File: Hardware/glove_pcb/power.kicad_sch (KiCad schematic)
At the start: 16 parts, among them J1 Barrel_Jack_Switch, U1 AP63205WU, U2 TCR2EF33_LMCT

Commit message: Made most of changes from meeting
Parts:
- added C42, C43: 0.1uF, Capacitor_SMD:C_0603_1608Metric_Pad1.08x0.95mm_HandSolder, symbol Device:C
- added R38: 10k, Resistor_SMD:R_0805_2012Metric_Pad1.20x1.40mm_HandSolder, symbol Device:R
- added SW1: SW_SPST, symbol Switch:SW_SPST
- C4: value 1mF -> 1000uF
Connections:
- net GND: now also C42.2, C43.2
- net MOTOR_AREF: now also C43.1
- net POT_AREF: now also C42.1
- net at J1.1: now also SW1.1 (A); no longer D1.2 (A)
- net MOTOR_VM renamed +12V
- net VCC_BT renamed +3.3V
- net VCC_UC renamed +5V
- net +5V: now also R38.2; no longer U2.3 (CONTROL)
- new net: R38.1, U2.3 (CONTROL)
- new net: D1.2 (A), SW1.2 (B)
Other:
- note added: "3.3V -> BT"
- note removed: "3.3V -> HC-05"
- moved on the sheet: J1

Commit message: Finish changes according to feedback
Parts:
- renumbered C42 to C6, C43 to C7, C6 to C8, C7 to C9, R38 to R5

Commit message: Finish schematic updates
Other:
- moved on the sheet: J1

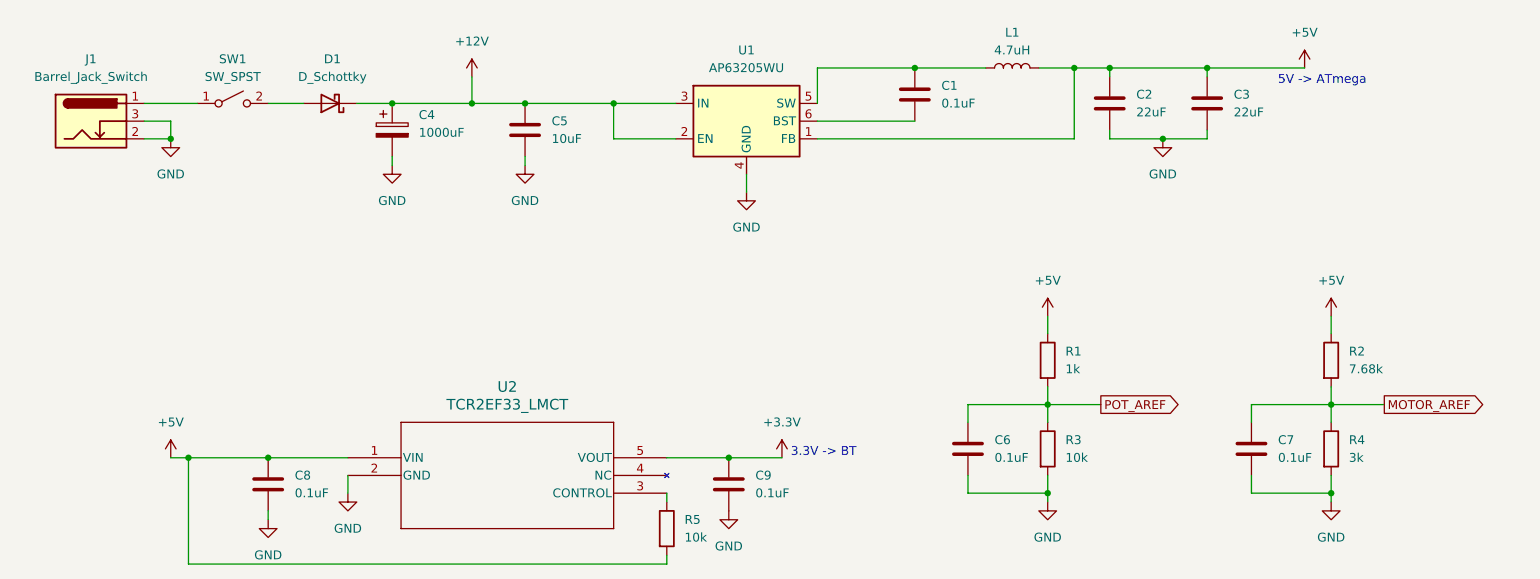
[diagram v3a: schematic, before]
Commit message: More updates to the schematic based on Dmitry's feedback
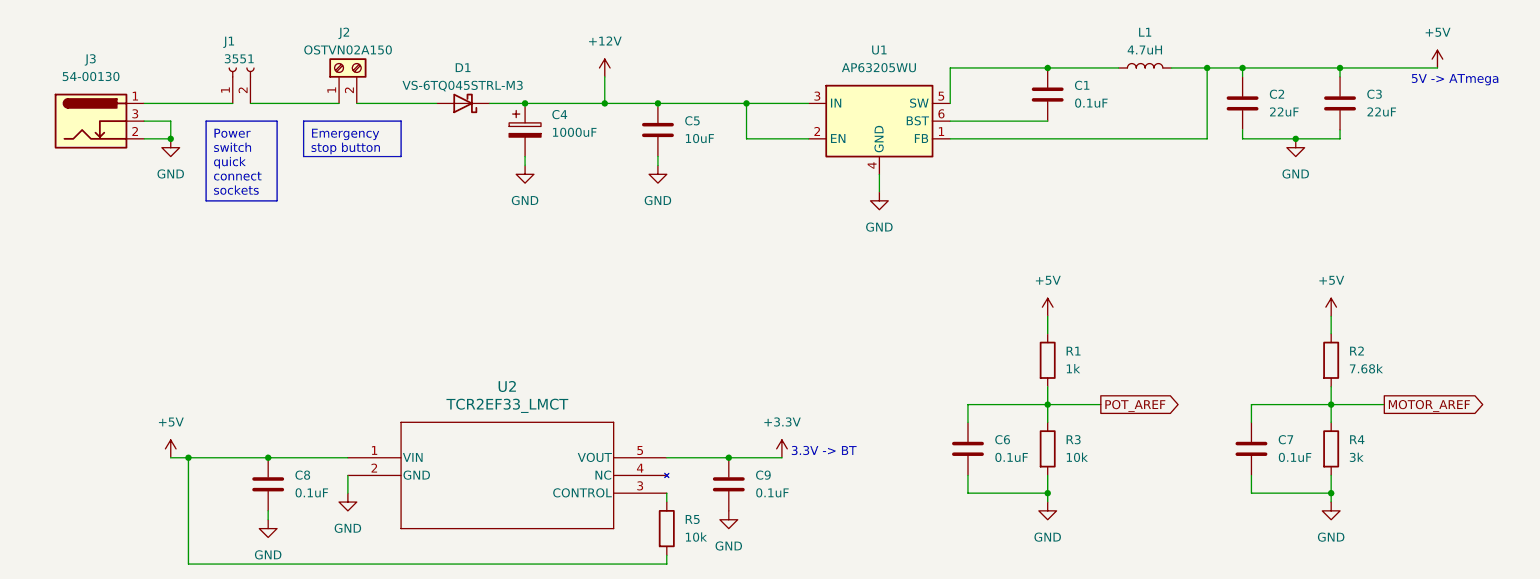
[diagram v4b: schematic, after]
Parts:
- removed SW1: SW_SPST, symbol Switch:SW_SPST
- added J1: 3551, symbol Connector:Conn_01x02_Socket
- added J2: OSTVN02A150, symbol Connector:Screw_Terminal_01x02
- D1: value D_Schottky -> VS-6TQ045STRL-M3
- J3: renamed from J1; value Barrel_Jack_Switch -> 54-00130
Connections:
- net at J3.1: now also J1.1 (Pin_1)
- net at D1.2 (A): now also J2.2 (Pin_2)
- new net: J1.2 (Pin_2), J2.1 (Pin_1)
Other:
- moved on the sheet: C1, C2, C3, C4, C5, D1, L1, U1
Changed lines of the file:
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@@
   (title_block
     (title "Power Supply")
-    (date "2023-11-24")
+    (date "2024-01-24")
     (company "COEN 490 Team 15")
   )

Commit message: Change isp pin symbol
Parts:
- U2: footprint SOT-25 SMV_TOS -> Glove_Footprints:SOT-25 SMV_TOS
